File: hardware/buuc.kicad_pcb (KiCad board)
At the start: 2 copper layers, 30.5 x 29.8 mm, 18 parts, among them J1 RADIO+, J2 RADIO-, P1 USB_OTG, Q1 NDS8434, U1 BOOST_REGULATOR, U2 MCP73842-840I/UN

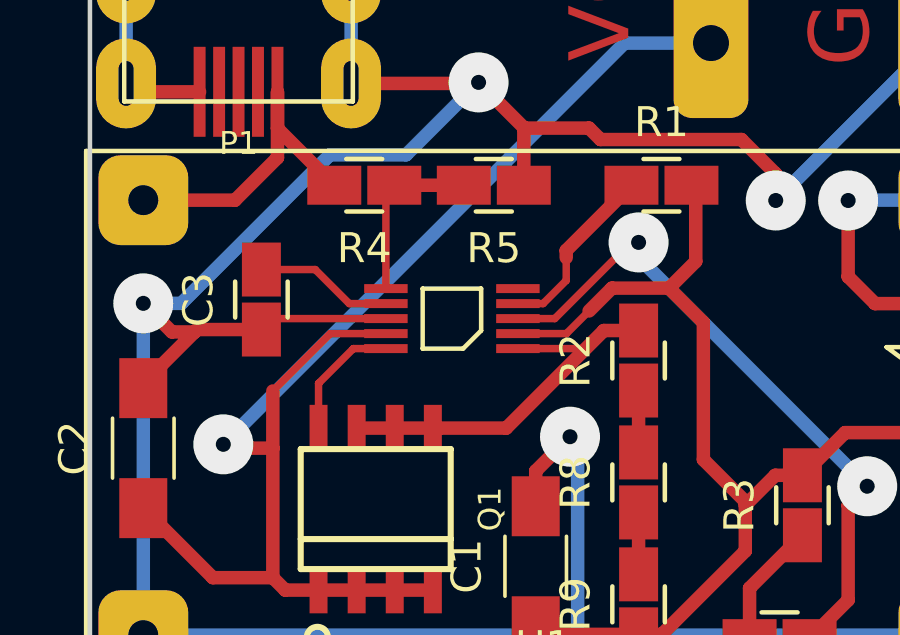
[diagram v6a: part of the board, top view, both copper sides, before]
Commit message: Updating to use slightly-wider tracks.
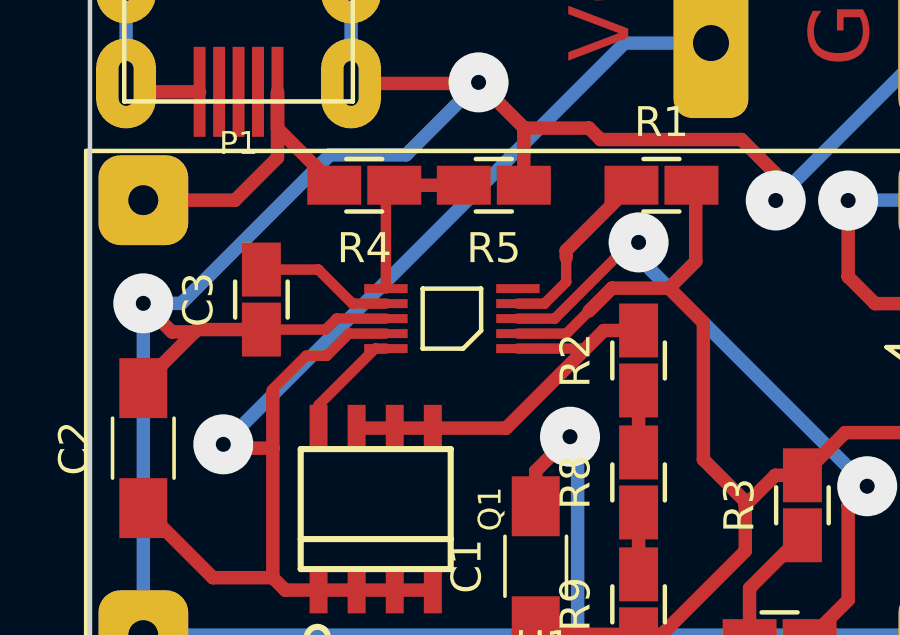
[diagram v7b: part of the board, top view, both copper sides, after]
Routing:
- net GND: track 120.6 -> 121.1 mm
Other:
- net class Default: clearance 0.2 -> 0.1
- rule trace_clearance: 0.2 -> 0.1
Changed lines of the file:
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@@
     (thickness 1.6)
     (drawings 6)
-    (tracks 128)
+    (tracks 135)
     (zones 0)
     (modules 18)
@@
   )
   (setup
-    (last_trace_width 0.45)
+    (last_trace_width 0.35)
     (user_trace_width 0.25)
     (user_trace_width 0.35)
-    (trace_clearance 0.2)
+    (trace_clearance 0.1)
     (zone_clearance 1)
     (zone_45_only yes)
@@
   (net 18 "Net-(R8-Pad1)")
   (net_class Default "This is the default net class."
-    (clearance 0.2)
+    (clearance 0.1)
     (trace_width 0.45)
     (via_dia 2)
@@
     (effects (font (size 2 2) (thickness 0.3)))
   )
+  (segment (start 75.86 52.062) (end 77.478 52.062) (width 0.35) (layer F.Cu) (net 1) (status 400000))
+  (segment (start 78.994 50.546) (end 80.899 50.546) (width 0.45) (layer F.Cu) (net 1))
+  (segment (start 78.232 51.308) (end 78.994 50.546) (width 0.45) (layer F.Cu) (net 1))
+  (segment (start 77.478 52.062) (end 78.232 51.308) (width 0.35) (layer F.Cu) (net 1))
   (segment (start 80.899 50.546) (end 81.788 49.657) (width 0.45) (layer F.Cu) (net 1))
   (segment (start 81.788 49.657) (end 81.788 47.26) (width 0.45) (layer F.Cu) (net 1) (status 800000))
   (segment (start 81.788 47.26) (end 81.645 47.117) (width 0.45) (layer F.Cu) (net 1) (status C00000))
-  (segment (start 78.232 51.308) (end 78.994 50.546) (width 0.45) (layer F.Cu) (net 1))
-  (segment (start 77.478 52.062) (end 78.232 51.308) (width 0.25) (layer F.Cu) (net 1))
-  (segment (start 75.86 52.062) (end 77.478 52.062) (width 0.25) (layer F.Cu) (net 1) (status 400000))
   (segment (start 82.042 56.261) (end 83.5025 57.7215) (width 0.45) (layer F.Cu) (net 1))
   (segment (start 82.042 51.689) (end 82.042 56.261) (width 0.45) (layer F.Cu) (net 1))
   (segment (start 80.899 50.546) (end 82.042 51.689) (width 0.45) (layer F.Cu) (net 1))
-  (segment (start 78.994 50.546) (end 80.899 50.546) (width 0.45) (layer F.Cu) (net 1))
   (segment (start 90.043 55.363) (end 86.766 55.363) (width 0.45) (layer F.Cu) (net 1) (status 400000))
   (segment (start 86.766 55.363) (end 85.344 56.785) (width 0.45) (layer F.Cu) (net 1) (status 800000))
@@
   (segment (start 79.883 62.087) (end 76.724 62.087) (width 0.45) (layer F.Cu) (net 1) (status C00000))
   (segment (start 76.724 62.087) (end 76.454 61.817) (width 0.45) (layer F.Cu) (net 1) (status C00000))
+  (segment (start 67.31 51.927) (end 69.453 51.927) (width 0.35) (layer F.Cu) (net 2) (status 400000))
+  (segment (start 69.818 51.562) (end 71.46 51.562) (width 0.35) (layer F.Cu) (net 2) (status 800000))
+  (segment (start 69.453 51.927) (end 69.818 51.562) (width 0.35) (layer F.Cu) (net 2))
   (segment (start 70.298 40.223) (end 70.298 43.723) (width 0.45) (layer B.Cu) (net 2) (status C00000))
   (segment (start 62.798 40.223) (end 70.298 40.223) (width 0.45) (layer B.Cu) (net 2) (status C00000))
@@
   (segment (start 76.057 45.212) (end 76.057 47.117) (width 0.45) (layer F.Cu) (net 2) (status 800000))
   (segment (start 89.789 37.378) (end 89.789 42.378) (width 0.45) (layer B.Cu) (net 2) (status C00000))
-  (segment (start 71.46 51.562) (end 67.675 51.562) (width 0.25) (layer F.Cu) (net 2) (status C00000))
   (segment (start 67.675 51.562) (end 67.31 51.927) (width 0.25) (layer F.Cu) (net 2) (status C00000))
   (segment (start 65.25006 44.00296) (end 63.07796 44.00296) (width 0.45) (layer F.Cu) (net 2) (status C00000))
   (segment (start 63.07796 44.00296) (end 62.798 43.723) (width 0.45) (layer F.Cu) (net 2) (status C00000))
+  (segment (start 67.691 53.975) (end 67.691 53.909) (width 0.35) (layer F.Cu) (net 3))
+  (segment (start 67.691 55.88) (end 67.691 53.975) (width 0.45) (layer F.Cu) (net 3))
+  (segment (start 70.228 52.062) (end 71.46 52.062) (width 0.35) (layer F.Cu) (net 3) (status 800000))
+  (segment (start 69.49 52.8) (end 70.228 52.062) (width 0.35) (layer F.Cu) (net 3))
+  (segment (start 68.8 52.8) (end 69.49 52.8) (width 0.35) (layer F.Cu) (net 3))
+  (segment (start 67.691 53.909) (end 68.8 52.8) (width 0.35) (layer F.Cu) (net 3))
   (segment (start 67.691 55.88) (end 66.167 55.88) (width 0.45) (layer F.Cu) (net 3))
   (segment (start 79.415 42.378) (end 82.296 42.378) (width 0.45) (layer B.Cu) (net 3) (status 800000))
@@
   (segment (start 70.485 60.612) (end 71.755 60.612) (width 0.45) (layer F.Cu) (net 3) (status C00000))
   (segment (start 69.215 60.612) (end 70.485 60.612) (width 0.45) (layer F.Cu) (net 3) (status C00000))
-  (segment (start 67.691 53.975) (end 67.691 55.88) (width 0.45) (layer F.Cu) (net 3))
   (segment (start 67.691 55.88) (end 67.691 60.198) (width 0.45) (layer F.Cu) (net 3))
-  (segment (start 69.604 52.062) (end 67.691 53.975) (width 0.25) (layer F.Cu) (net 3))
-  (segment (start 71.46 52.062) (end 69.604 52.062) (width 0.25) (layer F.Cu) (net 3) (status 400000))
   (segment (start 68.105 60.612) (end 69.215 60.612) (width 0.45) (layer F.Cu) (net 3) (status 800000))
   (segment (start 67.691 60.198) (end 68.105 60.612) (width 0.45) (layer F.Cu) (net 3))
-  (segment (start 69.215 55.212) (end 69.215 53.721) (width 0.25) (layer F.Cu) (net 4) (status 400000))
-  (segment (start 70.374 52.562) (end 71.46 52.562) (width 0.25) (layer F.Cu) (net 4) (status 800000))
-  (segment (start 69.215 53.721) (end 70.374 52.562) (width 0.25) (layer F.Cu) (net 4))
+  (segment (start 69.215 55.212) (end 69.215 54.445) (width 0.35) (layer F.Cu) (net 4) (status C00000))
+  (segment (start 69.215 54.445) (end 71.098 52.562) (width 0.35) (layer F.Cu) (net 4) (status C00000))
+  (segment (start 71.098 52.562) (end 71.46 52.562) (width 0.35) (layer F.Cu) (net 4) (status C00000))
+  (segment (start 75.86 52.562) (end 78.121 52.562) (width 0.35) (layer F.Cu) (net 5) (status 400000))
+  (segment (start 78.121 52.562) (end 78.724 51.959) (width 0.25) (layer F.Cu) (net 5))
   (segment (start 73.025 55.212) (end 75.471 55.212) (width 0.45) (layer F.Cu) (net 5) (status 400000))
   (segment (start 75.471 55.212) (end 78.724 51.959) (width 0.45) (layer F.Cu) (net 5))
@@
   (segment (start 73.246 55.212) (end 73.025 55.212) (width 0.45) (layer F.Cu) (net 5) (status C00000))
   (segment (start 70.485 55.212) (end 71.755 55.212) (width 0.45) (layer F.Cu) (net 5) (status C00000))
-  (segment (start 75.86 52.562) (end 78.121 52.562) (width 0.25) (layer F.Cu) (net 5) (status 400000))
-  (segment (start 78.121 52.562) (end 78.724 51.959) (width 0.25) (layer F.Cu) (net 5))
   (segment (start 78.724 51.959) (end 79.883 51.959) (width 0.25) (layer F.Cu) (net 5) (status 800000))
+  (segment (start 75.86 51.062) (end 76.748 51.062) (width 0.35) (layer F.Cu) (net 7) (status 400000))
+  (segment (start 77.47 49.292) (end 79.645 47.117) (width 0.45) (layer F.Cu) (net 7) (status 800000))
   (segment (start 77.47 49.53) (end 77.47 49.292) (width 0.45) (layer F.Cu) (net 7))
-  (segment (start 76.7 51.062) (end 77.47 50.292) (width 0.25) (layer F.Cu) (net 7))
-  (segment (start 77.47 50.292) (end 77.47 49.53) (width 0.25) (layer F.Cu) (net 7))
-  (segment (start 75.86 51.062) (end 76.7 51.062) (width 0.25) (layer F.Cu) (net 7) (status 400000))
-  (segment (start 77.47 49.292) (end 79.645 47.117) (width 0.45) (layer F.Cu) (net 7) (status 800000))
+  (segment (start 77.47 50.34) (end 77.47 49.53) (width 0.35) (layer F.Cu) (net 7))
+  (segment (start 76.748 51.062) (end 77.47 50.34) (width 0.35) (layer F.Cu) (net 7))
+  (segment (start 75.86 51.562) (end 77.088 51.562) (width 0.35) (layer F.Cu) (net 8) (status 400000))
+  (segment (start 79.628 49.022) (end 79.883 49.022) (width 0.35) (layer F.Cu) (net 8))
+  (segment (start 77.088 51.562) (end 79.628 49.022) (width 0.35) (layer F.Cu) (net 8))
   (segment (start 79.883 49.022) (end 79.883 49.53) (width 0.45) (layer B.Cu) (net 8))
-  (segment (start 77.089 51.562) (end 79.629 49.022) (width 0.25) (layer F.Cu) (net 8))
   (segment (start 79.629 49.022) (end 79.883 49.022) (width 0.25) (layer F.Cu) (net 8))
   (via (at 79.883 49.022) (size 2) (drill 0.5) (layers F.Cu B.Cu) (net 8))
-  (segment (start 75.86 51.562) (end 77.089 51.562) (width 0.25) (layer F.Cu) (net 8) (status 400000))
   (segment (start 86.868 60.944) (end 85.582 62.23) (width 0.45) (layer F.Cu) (net 8) (status 800000))
   (segment (start 86.868 57.785) (end 86.868 60.944) (width 0.45) (layer F.Cu) (net 8))
@@
   (segment (start 83.582 62.23) (end 83.582 60.547) (width 0.45) (layer F.Cu) (net 14) (status 400000))
   (segment (start 83.582 60.547) (end 85.344 58.785) (width 0.45) (layer F.Cu) (net 14) (status 800000))
-  (segment (start 71.46 51.062) (end 70.239 51.062) (width 0.25) (layer F.Cu) (net 15) (status 400000))
-  (segment (start 69.104 49.927) (end 67.31 49.927) (width 0.25) (layer F.Cu) (net 15) (status 800000))
-  (segment (start 70.239 51.062) (end 69.104 49.927) (width 0.25) (layer F.Cu) (net 15))
+  (segment (start 71.46 51.062) (end 70.342 51.062) (width 0.35) (layer F.Cu) (net 15) (status 400000))
+  (segment (start 69.207 49.927) (end 67.31 49.927) (width 0.35) (layer F.Cu) (net 15) (status 800000))
+  (segment (start 70.342 51.062) (end 69.207 49.927) (width 0.35) (layer F.Cu) (net 15))
+  (segment (start 71.46 50.562) (end 71.46 47.396) (width 0.35) (layer F.Cu) (net 16) (status C00000))
+  (segment (start 71.46 47.396) (end 71.739 47.117) (width 0.35) (layer F.Cu) (net 16) (status C00000))
   (segment (start 71.739 47.117) (end 74.057 47.117) (width 0.45) (layer F.Cu) (net 16) (status C00000))
-  (segment (start 71.46 50.562) (end 71.46 47.396) (width 0.25) (layer F.Cu) (net 16) (status C00000))
   (segment (start 71.46 47.396) (end 71.739 47.117) (width 0.25) (layer F.Cu) (net 16) (status C00000))
   (segment (start 79.883 56.023) (end 79.883 53.959) (width 0.45) (layer F.Cu) (net 17) (status C00000))
